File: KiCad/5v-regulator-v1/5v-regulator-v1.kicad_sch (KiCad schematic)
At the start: 54 parts, among them J1 Screw_Terminal_01x02, J2 USB-A1SSW6, J3 USB-A1SSW6, J4 USB-A1SSW6, J5 USB-A1SSW6, J6 Screw_Terminal_01x04, J7 Conn_01x04_Pin, Q1 Q_Dual_NMOS_S1G1D2S2G2D1, U1 TPS51386RJNR, U2 INA219AIDR, U3 INA219AIDR

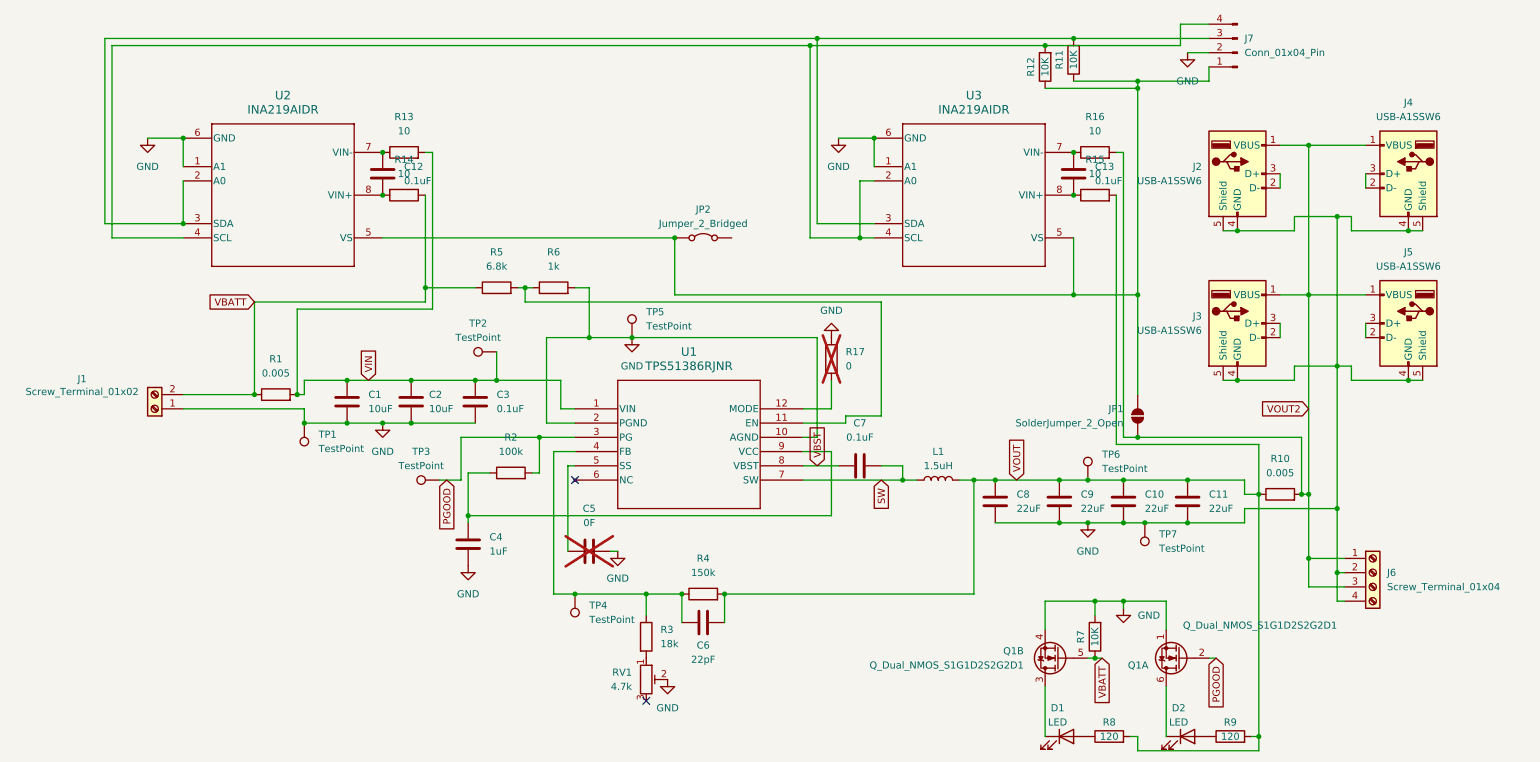
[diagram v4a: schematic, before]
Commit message: Added solder pad for LEDs
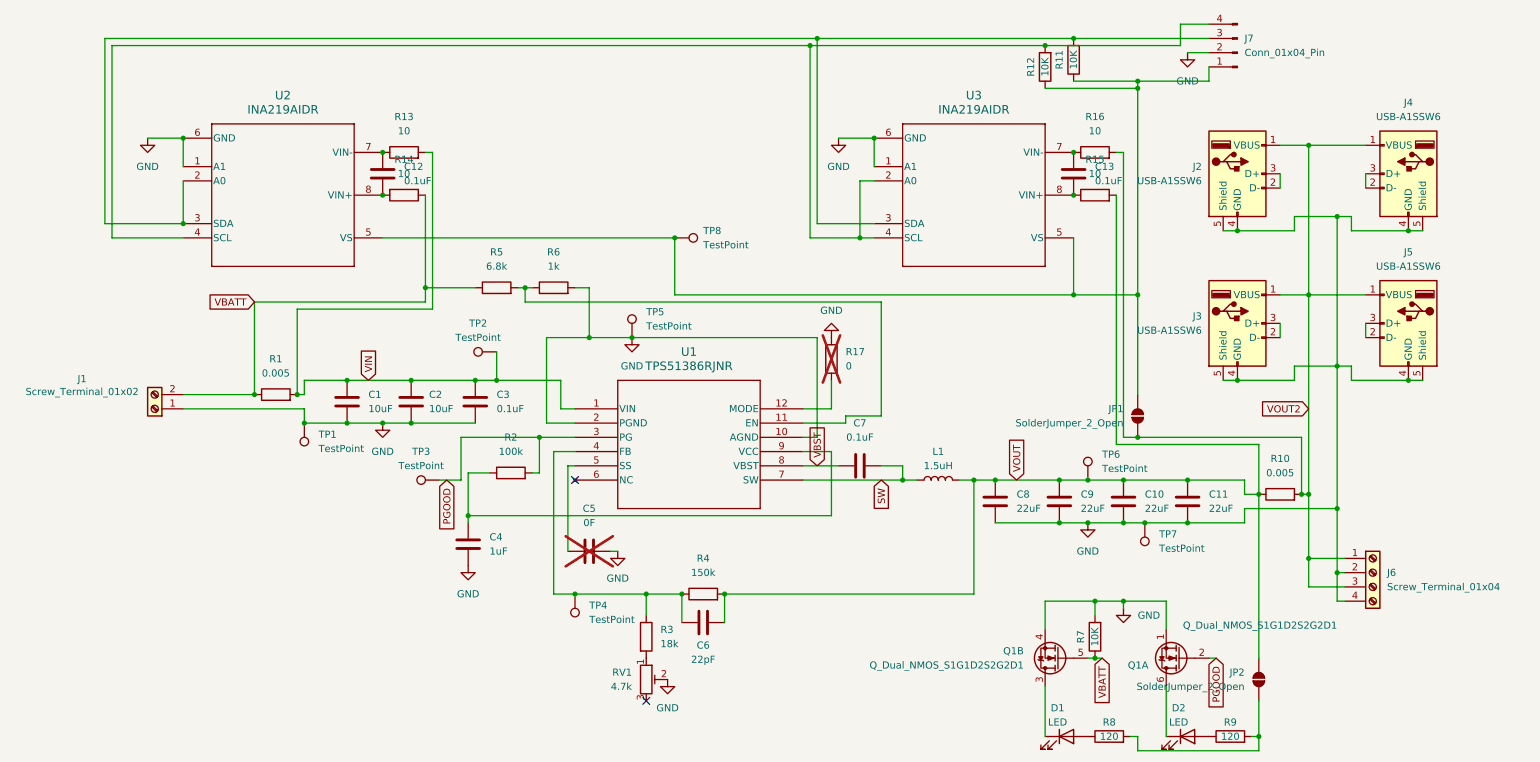
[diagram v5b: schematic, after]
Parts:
- removed JP2: Jumper_2_Bridged, TPS51386:usb_symbol, symbol Jumper:Jumper_2_Bridged
- added JP2: SolderJumper_2_Open, Jumper:SolderJumper-2_P1.3mm_Open_TrianglePad1.0x1.5mm, symbol Jumper:SolderJumper_2_Open
- added TP8: TestPoint, TPS51386:usb_symbol, symbol Connector:TestPoint
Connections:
- net VOUT: now also JP2.2 (B); no longer R8.2, R9.2
- net at J7.1 (Pin_1), JP1.2 (B), R11.1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: now also TP8.1
- new net: JP2.1 (A), R8.2, R9.2
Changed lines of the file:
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@@
 	)
 	(junction
-		(at 130.81 62.23)
-		(diameter 0)
-		(color 0 0 0 0)
-	)
-	(junction
 		(at 72.39 95.25)
 		(diameter 0)
@@
 	)
 	(junction
+		(at 130.81 62.23)
+		(diameter 0)
+		(color 0 0 0 0)
+	)
+	(junction
 		(at 171.45 105.41)
 		(diameter 0)
@@
 	(wire
 		(pts
+			(xy 234.95 107.95) (xy 234.95 137.16)
+		)
+		(stroke
+			(width 0)
+			(type default)
+		)
+	)
+	(wire
+		(pts
 			(xy 228.6 87.63) (xy 231.14 87.63)
 		)
@@
 	(wire
 		(pts
+			(xy 234.95 144.78) (xy 234.95 151.13)
+		)
+		(stroke
+			(width 0)
+			(type default)
+		)
+	)
+	(wire
+		(pts
 			(xy 43.18 62.23) (xy 30.48 62.23)
 		)
@@
 	(wire
 		(pts
-			(xy 234.95 107.95) (xy 234.95 151.13)
-		)
-		(stroke
-			(width 0)
-			(type default)
-		)
-	)
-	(wire
-		(pts
 			(xy 92.71 105.41) (xy 92.71 97.79)
 		)
@@
 	)
 	(symbol
+		(lib_id "Connector:TestPoint")
+		(at 130.81 62.23 270)
+		(unit 1)
+		(exclude_from_sim no)
+		(in_bom yes)
+		(on_board yes)
+		(dnp no)
+		(fields_autoplaced yes)
+		(property "Reference" "TP8"
+			(at 135.89 60.9599 90)
+			(effects
+				(font
+					(size 1.27 1.27)
+				)
+				(justify left)
+			)
+		)
+		(property "Value" "TestPoint"
+			(at 135.89 63.4999 90)
+			(effects
+				(font
+					(size 1.27 1.27)
+				)
+				(justify left)
+			)
+		)
+		(property "Footprint" "TPS51386:usb_symbol"
+			(at 130.81 67.31 0)
+			(effects
+				(font
+					(size 1.27 1.27)
+				)
+				(hide yes)
+			)
+		)
+		(property "Datasheet" "~"
+			(at 130.81 67.31 0)
+			(effects
+				(font
+					(size 1.27 1.27)
+				)
+				(hide yes)
+			)
+		)
+		(property "Description" "test point"
+			(at 130.81 62.23 0)
+			(effects
+				(font
+					(size 1.27 1.27)
+				)
+				(hide yes)
+			)
+		)
+		(pin "1"
+		)
+		(instances
+			(project "5v-regulator-v1"
+				(path "/4305ae50-7d96-42de-9eb2-54fda8fc6884"
+					(reference "TP8")
+					(unit 1)
+				)
+			)
+		)
+	)
+	(symbol
 		(lib_id "TPS51386RJNR:TPS51386RJNR")
 		(at 113.03 92.71 0)
@@
 	)
 	(symbol
-		(lib_id "Jumper:Jumper_2_Bridged")
-		(at 135.89 62.23 0)
-		(unit 1)
-		(exclude_from_sim yes)
-		(in_bom yes)
-		(on_board yes)
-		(dnp no)
-		(fields_autoplaced yes)
-		(property "Reference" "JP2"
-			(at 135.89 57.15 0)
-			(effects
-				(font
-					(size 1.27 1.27)
-				)
-			)
-		)
-		(property "Value" "Jumper_2_Bridged"
-			(at 135.89 59.69 0)
-			(effects
-				(font
-					(size 1.27 1.27)
-				)
-			)
-		)
-		(property "Footprint" "TPS51386:usb_symbol"
-			(at 135.89 62.23 0)
-			(effects
-				(font
-					(size 1.27 1.27)
-				)
-				(hide yes)
-			)
-		)
-		(property "Datasheet" "~"
-			(at 135.89 62.23 0)
-			(effects
-				(font
-					(size 1.27 1.27)
-				)
-				(hide yes)
-			)
-		)
-		(property "Description" "Jumper, 2-pole, closed/bridged"
-			(at 135.89 62.23 0)
-			(effects
-				(font
-					(size 1.27 1.27)
-				)
-				(hide yes)
-			)
-		)
-		(pin "2"
-		)
-		(pin "1"
-		)
-		(instances
-			(project "5v-regulator-v1"
-				(path "/4305ae50-7d96-42de-9eb2-54fda8fc6884"
-					(reference "JP2")
-					(unit 1)
-				)
-			)
-		)
-	)
-	(symbol
 		(lib_id "Device:C")
 		(at 222.25 109.22 0)
@@
 					(unit 1)
 				)
+			)
+		)
+	)
+	(symbol
+		(lib_id "Jumper:SolderJumper_2_Open")
+		(at 234.95 140.97 270)
+		(mirror x)
+		(unit 1)
+		(exclude_from_sim yes)
+		(in_bom no)
+		(on_board yes)
+		(dnp no)
+		(property "Reference" "JP2"
+			(at 232.41 139.6999 90)
+			(effects
+				(font
+					(size 1.27 1.27)
+				)
+				(justify right)
+			)
+		)
+		(property "Value" "SolderJumper_2_Open"
+			(at 232.41 142.2399 90)
+			(effects
+				(font
+					(size 1.27 1.27)
+				)
+				(justify right)
+			)
+		)
+		(property "Footprint" "Jumper:SolderJumper-2_P1.3mm_Open_TrianglePad1.0x1.5mm"
+			(at 234.95 140.97 0)
+			(effects
+				(font
+					(size 1.27 1.27)
+				)
+				(hide yes)
+			)
+		)
+		(property "Datasheet" "~"
+			(at 234.95 140.97 0)
+			(effects
+				(font
+					(size 1.27 1.27)
+				)
+				(hide yes)
+			)
+		)
+		(property "Description" "Solder Jumper, 2-pole, open"
+			(at 234.95 140.97 0)
+			(effects
+				(font
+					(size 1.27 1.27)
+				)
+				(hide yes)
+			)
+		)
+		(pin "2"
+		)
+		(pin "1"
+		)
+		(instances
+			(project "5v-regulator-v1"
+				(path "/4305ae50-7d96-42de-9eb2-54fda8fc6884"
+					(reference "JP2")
+					(unit 1)
+				)

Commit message: Increased pitch of terminal blocks to fit ferrules
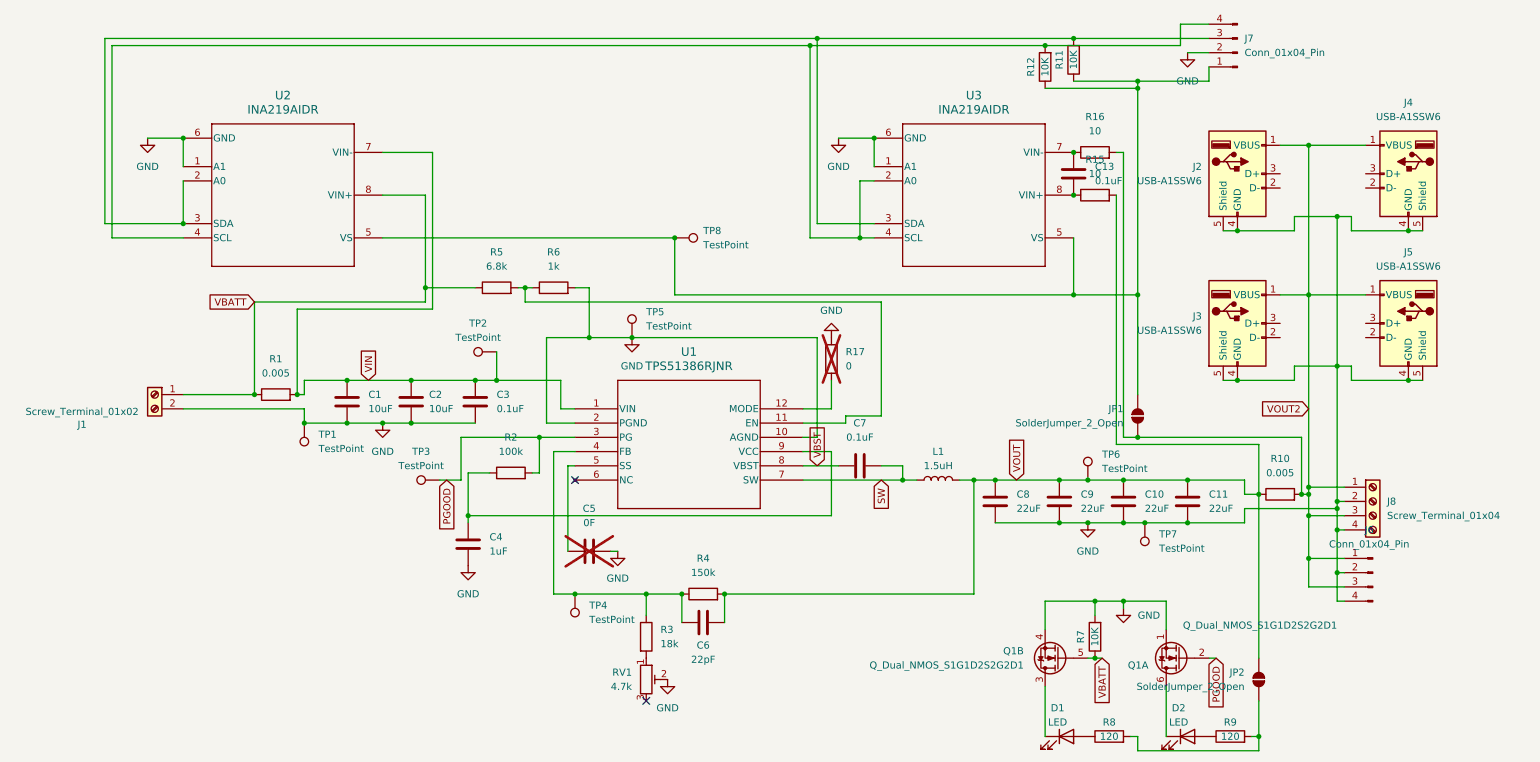
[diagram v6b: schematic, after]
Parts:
- removed C12: 0.1uF, Capacitor_SMD:C_1206_3216Metric_Pad1.33x1.80mm_HandSolder, symbol Device:C
- removed R13, R14: 10, Resistor_SMD:R_1206_3216Metric_Pad1.30x1.75mm_HandSolder, symbol Device:R
- added J8: Screw_Terminal_01x04, TerminalBlock:TerminalBlock_bornier-4_P5.08mm, symbol Connector:Screw_Terminal_01x04
- J1: footprint TerminalBlock:TerminalBlock_Xinya_XY308-2.54-2P_1x02_P2.54mm_Horizontal -> TerminalBlock:TerminalBlock_bornier-2_P5.08mm
- J6: value Screw_Terminal_01x04 -> Conn_01x04_Pin; footprint TerminalBlock:TerminalBlock_Xinya_XY308-2.54-4P_1x04_P2.54mm_Horizontal -> Connector_PinHeader_2.54mm:PinHeader_1x04_P2.54mm_Vertical; symbol Connector:Screw_Terminal_01x04 -> Connector:Conn_01x04_Pin
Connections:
- net GND: now also J1.2 (Pin_2), J8.2 (Pin_2), J8.4 (Pin_4); no longer J1.1 (Pin_1)
- net VBATT: now also J1.1 (Pin_1), U2.8 (VIN+); no longer J1.2 (Pin_2)
- net VIN: now also U2.7 (VIN-)
- net VOUT2: now also J8.1 (Pin_1), J8.3 (Pin_3)
- net at J4.2 (D-): no longer J4.3 (D+)
- net at J5.2 (D-): no longer J5.3 (D+)
- net at J2.2 (D-): no longer J2.3 (D+)
- net at J3.2 (D-): no longer J3.3 (D+)
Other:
- moved on the sheet: J1

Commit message: Added input fuse and switched to stacked USBs
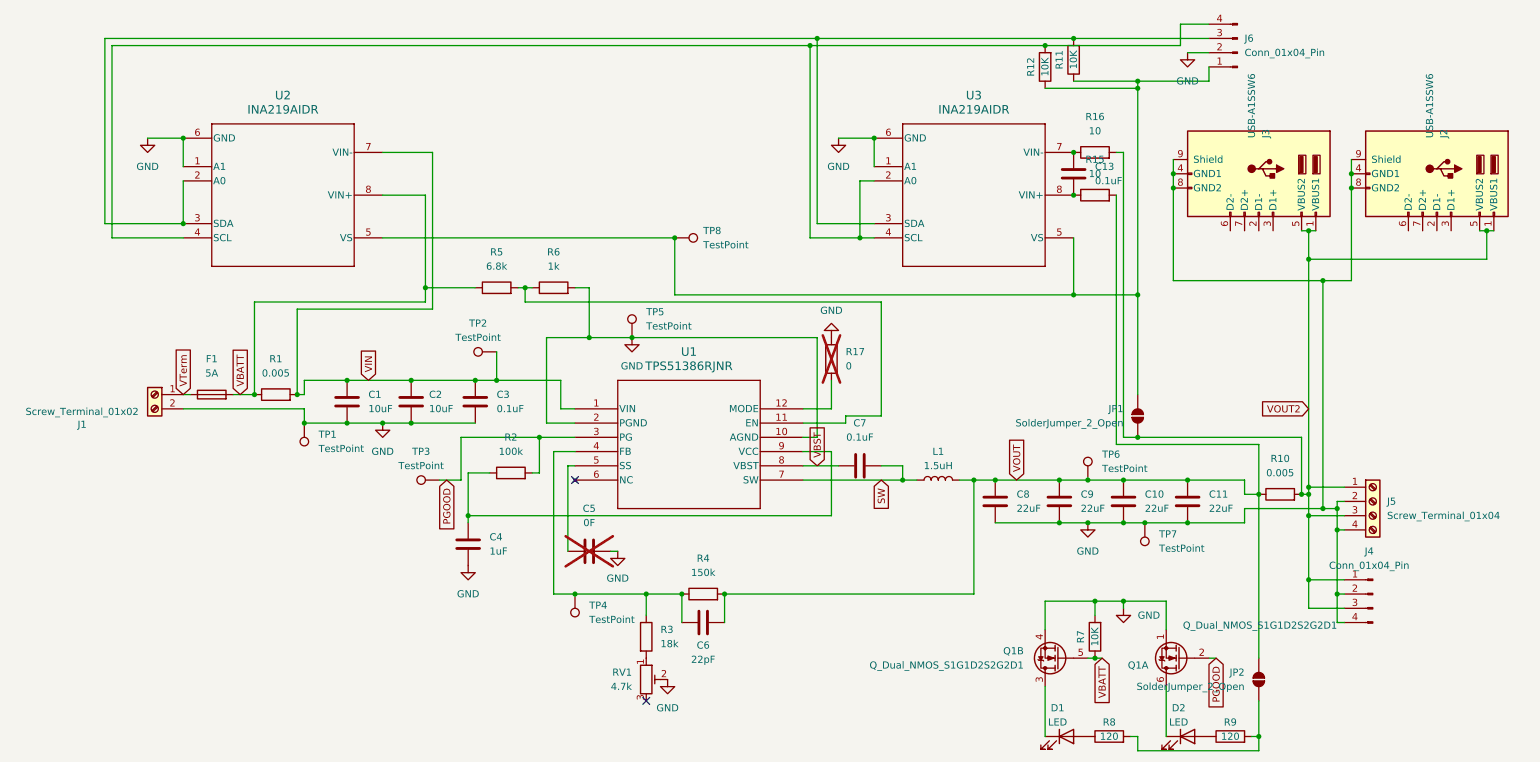
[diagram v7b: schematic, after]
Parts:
- removed J4, J5: USB-A1SSW6, Connector_USB:USB_A_Wuerth_614004134726_Horizontal, symbol Connector:USB_A
- added F1: 5A, Fuse:Fuse_0603_1608Metric_Pad1.05x0.95mm_HandSolder, symbol Device:Fuse
- J2, J3: footprint Connector_USB:USB_A_Wuerth_614004134726_Horizontal -> Connector_USB:USB_A_Wuerth_61400826021_Horizontal_Stacked; symbol Connector:USB_A -> Connector:USB_A_Stacked
- renumbered J6 to J4, J8 to J5, J7 to J6
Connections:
- net GND: now also J2.8 (GND2), J2.9 (Shield), J3.8 (GND2), J3.9 (Shield); no longer J2.5 (Shield), J3.5 (Shield)
- net VBATT: now also F1.2; no longer J1.1 (Pin_1)
- net VOUT2: now also J2.5 (VBUS2), J3.5 (VBUS2)
- new net VTerm: F1.1, J1.1 (Pin_1)
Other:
- moved on the sheet: J4

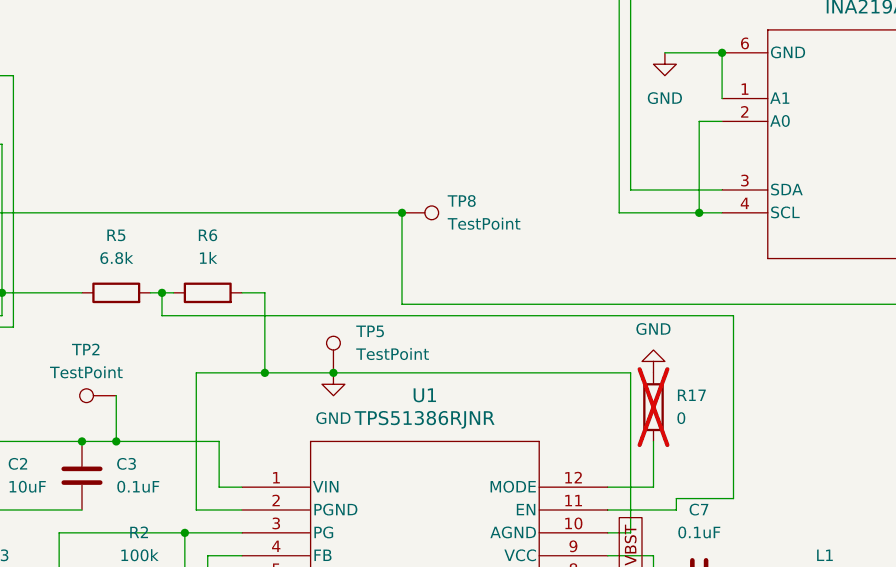
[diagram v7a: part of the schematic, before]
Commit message: Updated battery meter with 2S values
Need to figure out a good way to automatically calculate resistor values based on input voltages...
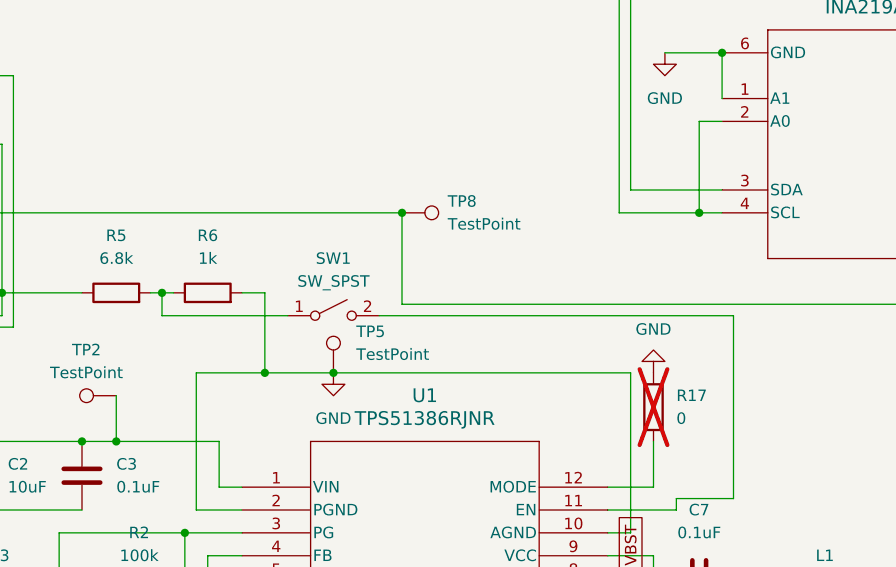
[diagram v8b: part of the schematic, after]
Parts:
- added SW1: SW_SPST, symbol Switch:SW_SPST
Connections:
- net at R5.2, R6.1: now also SW1.1 (A); no longer U1.11 (EN)
- new net: SW1.2 (B), U1.11 (EN)
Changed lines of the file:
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@@
+	(wire
+		(pts
+			(xy 128.27 73.66) (xy 167.64 73.66)
+		)
+		(stroke
+			(width 0)
+			(type default)
+		)
+	)
 	(wire
 		(pts
@@
 	(wire
 		(pts
-			(xy 104.14 73.66) (xy 167.64 73.66)
-		)
-		(stroke
-			(width 0)
-			(type default)
-		)
-	)
-	(wire
-		(pts
 			(xy 218.44 127) (xy 218.44 132.08)
 		)
@@
 		(pts
 			(xy 102.87 71.12) (xy 104.14 71.12)
+		)
+		(stroke
+			(width 0)
+			(type default)
+		)
+	)
+	(wire
+		(pts
+			(xy 104.14 73.66) (xy 118.11 73.66)
 		)
 		(stroke
@@
 					(unit 1)
 				)
+			)
+		)
+	)
+	(symbol
+		(lib_id "Switch:SW_SPST")
+		(at 123.19 73.66 0)
+		(unit 1)
+		(exclude_from_sim no)
+		(in_bom yes)
+		(on_board yes)
+		(dnp no)
+		(fields_autoplaced yes)
+		(property "Reference" "SW1"
+			(at 123.19 67.31 0)
+			(effects
+				(font
+					(size 1.27 1.27)
+				)
+			)
+		)
+		(property "Value" "SW_SPST"
+			(at 123.19 69.85 0)
+			(effects
+				(font
+					(size 1.27 1.27)
+				)
+			)
+		)
+		(property "Footprint" ""
+			(at 123.19 73.66 0)
+			(effects
+				(font
+					(size 1.27 1.27)
+				)
+				(hide yes)
+			)
+		)
+		(property "Datasheet" "~"
+			(at 123.19 73.66 0)
+			(effects
+				(font
+					(size 1.27 1.27)
+				)
+				(hide yes)
+			)
+		)
+		(property "Description" "Single Pole Single Throw (SPST) switch"
+			(at 123.19 73.66 0)
+			(effects
+				(font
+					(size 1.27 1.27)
+				)
+				(hide yes)
+			)
+		)
+		(pin "1"
+		)
+		(pin "2"
+		)
+		(instances
+			(project "5v-regulator-v1"
+				(path "/4305ae50-7d96-42de-9eb2-54fda8fc6884"
+					(reference "SW1")
+					(unit 1)
+				)
